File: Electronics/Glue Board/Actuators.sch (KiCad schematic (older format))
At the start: 4 parts, among them Q1 CSD17501Q5A, U1 PCA9685PW, U2 DRV8870DDA, U3 VNH5019A-E

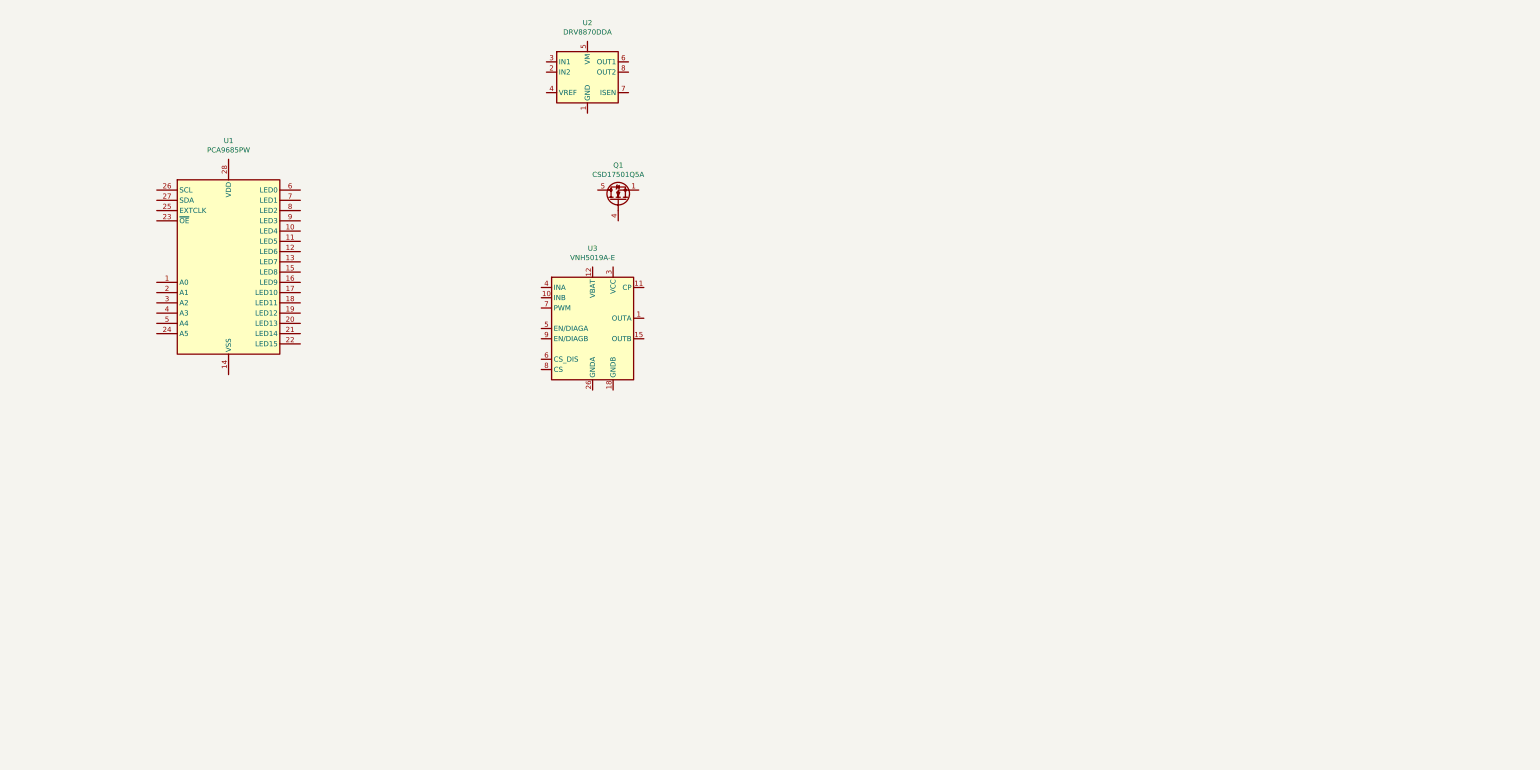
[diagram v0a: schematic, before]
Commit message: Finished the schematic for the most parts
Finished the schematic for the most parts
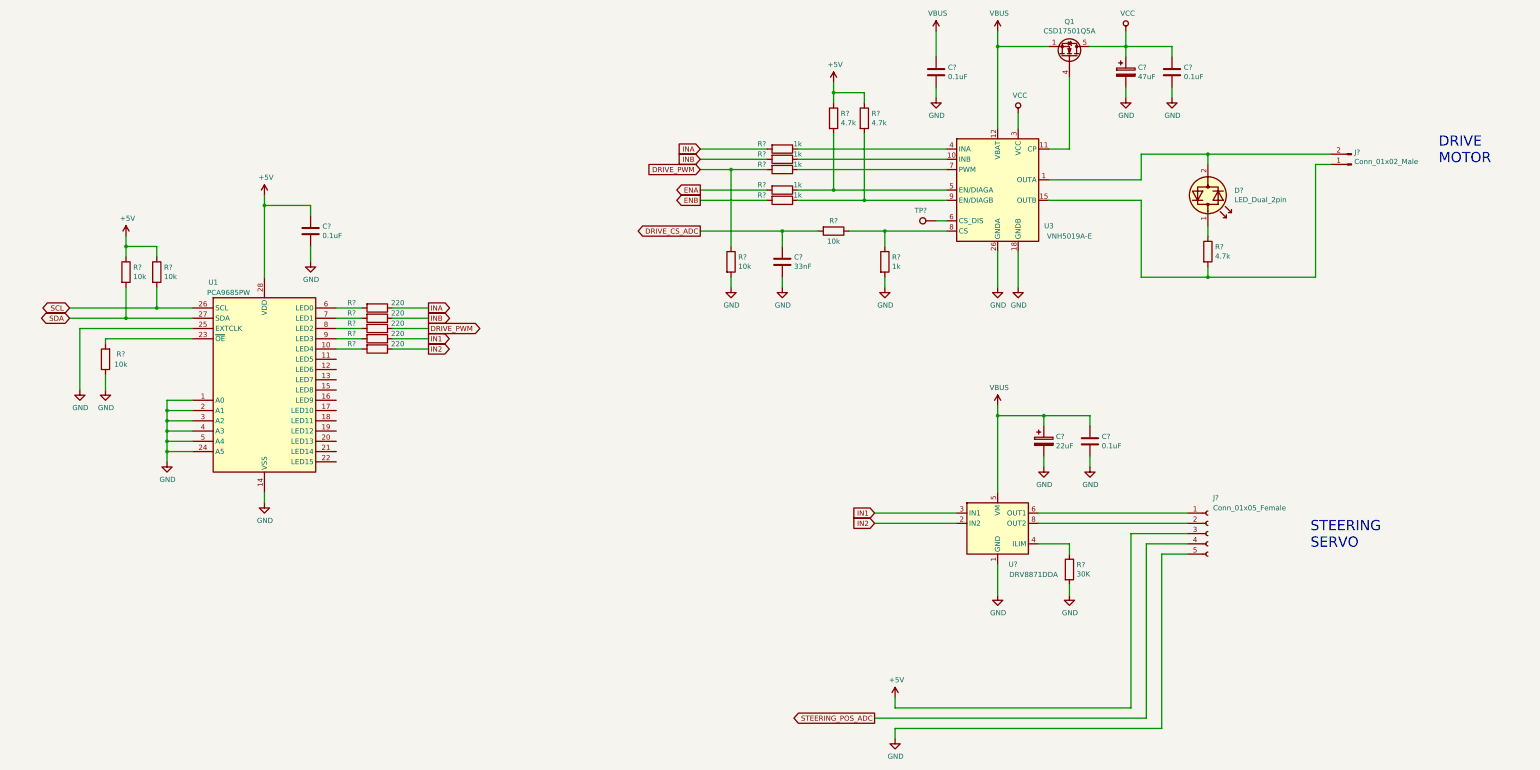
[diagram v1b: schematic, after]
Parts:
- removed U2: DRV8870DDA, Package_SO:Texas_HTSOP-8-1EP_3.9x4.9mm_P1.27mm_EP2.95x4.9mm_Mask2.4x3.1mm_ThermalVias, symbol Driver_Motor:DRV8870DDA
- added C?: 47uF, symbol Device:CP
- added C? (x4): 0.1uF, symbol Device:C
- added C?: 33nF, symbol Device:C
- added C?: 22uF, symbol Device:CP
- added D?: LED_Dual_2pin, symbol Device:LED_Dual_2pin
- added J?: Conn_01x02_Male, symbol Connector:Conn_01x02_Male
- added J?: Conn_01x05_Female, symbol Connector:Conn_01x05_Female
- added R? (x6): 1k, symbol Device:R
- added R? (x5): 10k, symbol Device:R
- added R? (x3): 4.7k, symbol Device:R
- added R?: 30K, symbol Device:R
- added R? (x5): 220, symbol Device:R
- added TP?: TestPoint, symbol Connector:TestPoint
- added U?: DRV8871DDA, Package_SO:Texas_HTSOP-8-1EP_3.9x4.9mm_P1.27mm_EP2.95x4.9mm_Mask2.4x3.1mm_ThermalVias, symbol Driver_Motor:DRV8871DDA
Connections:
- net GND: now reaches U1.1 (A0)
- net GND: now also U1.14 (VSS), U1.2 (A1), U1.24 (A5), U1.25 (EXTCLK), U1.3 (A2), U1.4 (A3), U1.5 (A4), U3.18 (GNDB), U3.19 (GNDB), U3.20 (GNDB), U3.26 (GNDA), U3.27 (GNDA), U3.28 (GNDA), C?.2, C?.2, C?.2, C?.2, C?.2, C?.2, C?.2, J?.5 (Pin_5), R?.1, R?.2, R?.2, R?.2, U?.1 (GND), U?.7 (GND), U?.9 (GND)
- net at U1.10 (LED4): now also R?.2
- net at U1.23 (~OE): now also R?.2
- net SCL: now reaches U1.26 (SCL)
- net SCL: now also R?.2
- net SDA: now reaches U1.27 (SDA)
- net SDA: now also R?.2
- net +5V: now reaches U1.28 (VDD)
- net +5V: now also C?.1, J?.3 (Pin_3), R?.1, R?.1, R?.1, R?.1
- net at U1.6 (LED0): now also R?.2
- net at U1.7 (LED1): now also R?.2
- net at U1.8 (LED2): now also R?.2
- net at U1.9 (LED3): now also R?.2
- net at U3.1 (OUTA), U3.25 (OUTA), U3.30 (OUTA)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: now also D?.2 (AK), J?.2 (Pin_2)
- net at U3.10 (INB): now also R?.1
- net at U3.11 (CP): now also Q1.4 (G)
- net VBUS: now reaches U3.12 (VBAT)
- net VBUS: now also Q1.1 (S), Q1.2 (S), Q1.3 (S), C?.1, C?.1, C?.1, U?.5 (VM)
- net VCC: now reaches U3.13 (VCC), U3.23 (VCC), U3.3 (VCC), U3.31 (VCC)
- net VCC: now also Q1.5 (D), C?.1, C?.1
- net at U3.15 (OUTB), U3.16 (OUTB), U3.21 (OUTB)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: now also J?.1 (Pin_1), R?.2
- net at U3.4 (INA): now also R?.1
- net at U3.5 (EN/DIAGA): now also R?.1, R?.2
- net at U3.6 (CS_DIS): now also TP?.1
- net at U3.7 (PWM): now also R?.1
- net at U3.8 (CS): now also R?.1, R?.1
- net at U3.9 (EN/DIAGB): now also R?.1, R?.2
- new net: D?.1 (KA), R?.1
- new net: R?.1, U?.4 (ILIM)
- new net: J?.1 (Pin_1), U?.6 (OUT1)
- new net: J?.2 (Pin_2), U?.8 (OUT2)
- new net DRIVE_CS_ADC: C?.1, R?.2
- new net DRIVE_PWM: R?.1, R?.1, R?.2
- new net ENA: R?.2
- new net ENB: R?.2
- new net IN1: R?.1, U?.3 (IN1)
- new net IN2: R?.1, U?.2 (IN2)
- new net INA: R?.1, R?.2
- new net INB: R?.1, R?.2
- new net STEERING_POS_ADC: J?.4 (Pin_4)
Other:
- note added: "DRIVE\nMOTOR"
- note added: "STEERING\nSERVO"
- moved on the sheet: Q1, U1, U3

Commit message: Complete Schematic and BOM
Complete Schematic and BOM. Next up, layout!
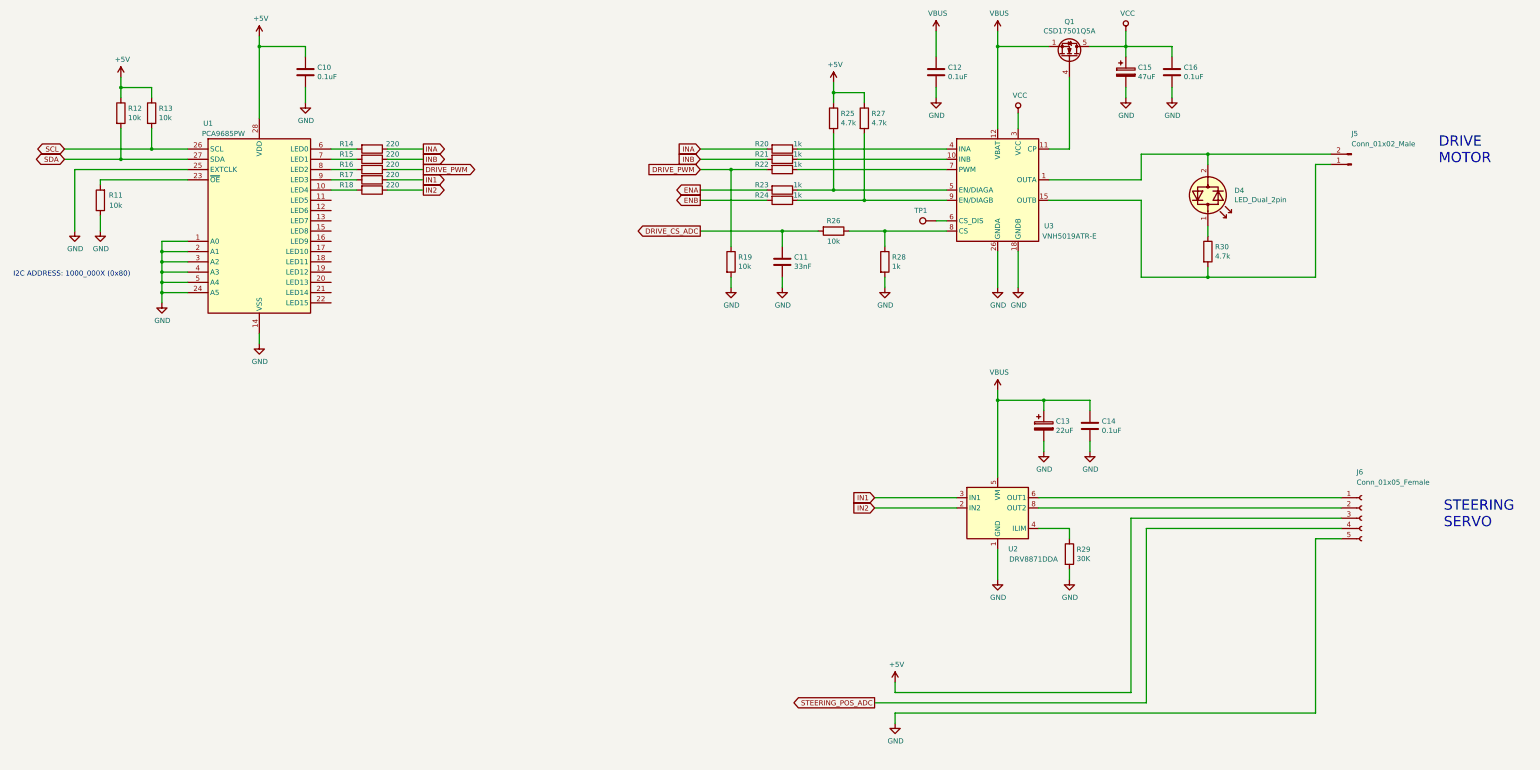
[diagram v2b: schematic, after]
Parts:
- C10, C12, C14, C16: renamed from C?; footprint (none) -> Capacitor_SMD:C_0805_2012Metric; MPN (none) -> C0805C104Z5VACTU
- C11: renamed from C?; footprint (none) -> Capacitor_SMD:C_0805_2012Metric; MPN (none) -> C0805C333K5RACTU
- C13: renamed from C?; footprint (none) -> Capacitor_SMD:C_1210_3225Metric; MPN (none) -> C1210C226K3PACTU
- C15: renamed from C?; footprint (none) -> Capacitor_SMD:C_1210_3225Metric; MPN (none) -> GRM32EC81C476KE15L
- D4: renamed from D?; footprint (none) -> LED_SMD:LED_1206_3216Metric; MPN (none) -> LTST-C235KGKRKT
- J5: renamed from J?; footprint (none) -> Connector_JST:JST_XH_B2B-XH-AM_1x02_P2.50mm_Vertical; MPN (none) -> B2B-XH-A(LF)(SN)
- J6: renamed from J?; footprint (none) -> Connector_Molex:Molex_PicoBlade_53047-0510_1x05_P1.25mm_Vertical; MPN (none) -> 0530470510
- Q1: MPN (none) -> CSD17501Q5A
- R11, R12, R13, R19, R26: renamed from R?; footprint (none) -> Resistor_SMD:R_0603_1608Metric; MPN (none) -> RC0603FR-0710KL
- R14, R15, R16, R17, R18: renamed from R?; footprint (none) -> Resistor_SMD:R_0603_1608Metric; MPN (none) -> CRGCQ0603F220R
- R20, R21, R22, R23, R24, R28: renamed from R?; footprint (none) -> Resistor_SMD:R_0603_1608Metric; MPN (none) -> RC0603JR-071KL
- R25, R27, R30: renamed from R?; footprint (none) -> Resistor_SMD:R_0603_1608Metric; MPN (none) -> ERJ-3EKF4751V
- R29: renamed from R?; footprint (none) -> Resistor_SMD:R_0603_1608Metric; MPN (none) -> ERA-3AEB303V
- TP1: renamed from TP?; footprint (none) -> TestPoint:TestPoint_Pad_D2.0mm
- U1: MPN (none) -> PCA9685PW
- U2: renamed from U?; MPN (none) -> DRV8871DDAR
- U3: value VNH5019A-E -> VNH5019ATR-E; MPN (none) -> VNH5019ATR-E
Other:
- note added: "I2C ADDRESS: 1000_000X (0x80)"
- moved on the sheet: C10, C13, C14, J6, R11, R12, R13, R14, R15, R16, R17, R18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

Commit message: Added Motor v-sense and battery mon. Layout time!
Added Motor v-sense and battery mon. Layout time!
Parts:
- removed R14, R15, R16, R17, R18: 220, Resistor_SMD:R_0603_1608Metric, symbol Device:R
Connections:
- net DRIVE_PWM: now also U1.8 (LED2)
- net IN1: now also U1.9 (LED3)
- net IN2: now also U1.10 (LED4)
- net INA: now also U1.6 (LED0)
- net INB: now also U1.7 (LED1)
- net OUTA: now reaches D4.2 (AK), U3.1 (OUTA), U3.25 (OUTA), U3.30 (OUTA), U3.33 (OUTA)
- net OUTA: now also J5.1 (Pin_1); no longer J5.2 (Pin_2)
- net OUTB: now reaches R30.2, U3.15 (OUTB), U3.16 (OUTB), U3.21 (OUTB), U3.32 (OUTB)
- net OUTB: now also J5.2 (Pin_2); no longer J5.1 (Pin_1)
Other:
- moved on the sheet: J5
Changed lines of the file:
@@
 L Connector:Conn_01x02_Male J5
 U 1 1 5E201F91
-P 14650 2700
-F 0 "J5" H 14650 2400 50  0000 R CNN
-F 1 "Conn_01x02_Male" H 14650 2500 50  0000 R CNN
-F 2 "Connector_JST:JST_XH_B2B-XH-AM_1x02_P2.50mm_Vertical" H 14650 2700 50  0001 C CNN
-F 3 "~" H 14650 2700 50  0001 C CNN
-F 4 "B2B-XH-A(LF)(SN)" H 14650 2700 50  0001 C CNN "MPN"
-	1    14650 2700
-	-1   0    0    1
+P 14700 2600
+F 0 "J5" H 14800 2800 50  0000 R CNN
+F 1 "Conn_01x02_Male" H 14800 2700 50  0000 R CNN
+F 2 "Connector_JST:JST_XH_B2B-XH-AM_1x02_P2.50mm_Vertical" H 14700 2600 50  0001 C CNN
+F 3 "~" H 14700 2600 50  0001 C CNN
+F 4 "B2B-XH-A(LF)(SN)" H 14700 2600 50  0001 C CNN "MPN"
+	1    14700 2600
+	-1   0    0    -1
 $EndComp
 $Comp
@@
 Wire Wire Line
 	13250 2700 13250 2600
-Connection ~ 13250 2600
 Wire Wire Line
 	13250 2600 12600 2600
@@
 Wire Wire Line
 	13250 3800 14300 3800
-Wire Wire Line
-	13250 2600 14450 2600
-Wire Wire Line
-	14450 2700 14300 2700
 Wire Wire Line
 	14300 2700 14300 3800
@@
 Wire Wire Line
 	4450 1950 4450 2100
-$Comp
-L Device:R R14
-U 1 1 5E2E4897
-P 5100 2550
-F 0 "R14" V 5050 2300 50  0000 C CNN
-F 1 "220" V 5050 2750 50  0000 C CNN
-F 2 "Resistor_SMD:R_0603_1608Metric" V 5030 2550 50  0001 C CNN
-F 3 "~" H 5100 2550 50  0001 C CNN
-F 4 "CRGCQ0603F220R" V 5100 2550 50  0001 C CNN "MPN"
-	1    5100 2550
-	0    1    1    0
-$EndComp
-$Comp
-L Device:R R15
-U 1 1 5E2E5029
-P 5100 2650
-F 0 "R15" V 5050 2400 50  0000 C CNN
-F 1 "220" V 5050 2850 50  0000 C CNN
-F 2 "Resistor_SMD:R_0603_1608Metric" V 5030 2650 50  0001 C CNN
-F 3 "~" H 5100 2650 50  0001 C CNN
-F 4 "CRGCQ0603F220R" V 5100 2650 50  0001 C CNN "MPN"
-	1    5100 2650
-	0    1    1    0
-$EndComp
-$Comp
-L Device:R R16
-U 1 1 5E2E53A1
-P 5100 2750
-F 0 "R16" V 5050 2500 50  0000 C CNN
-F 1 "220" V 5050 2950 50  0000 C CNN
-F 2 "Resistor_SMD:R_0603_1608Metric" V 5030 2750 50  0001 C CNN
-F 3 "~" H 5100 2750 50  0001 C CNN
-F 4 "CRGCQ0603F220R" V 5100 2750 50  0001 C CNN "MPN"
-	1    5100 2750
-	0    1    1    0
-$EndComp
-$Comp
-L Device:R R17
-U 1 1 5E2E5671
-P 5100 2850
-F 0 "R17" V 5050 2600 50  0000 C CNN
-F 1 "220" V 5050 3050 50  0000 C CNN
-F 2 "Resistor_SMD:R_0603_1608Metric" V 5030 2850 50  0001 C CNN
-F 3 "~" H 5100 2850 50  0001 C CNN
-F 4 "CRGCQ0603F220R" V 5100 2850 50  0001 C CNN "MPN"
-	1    5100 2850
-	0    1    1    0
-$EndComp
-$Comp
-L Device:R R18
-U 1 1 5E2E5899
-P 5100 2950
-F 0 "R18" V 5050 2700 50  0000 C CNN
-F 1 "220" V 5050 3150 50  0000 C CNN
-F 2 "Resistor_SMD:R_0603_1608Metric" V 5030 2950 50  0001 C CNN
-F 3 "~" H 5100 2950 50  0001 C CNN
-F 4 "CRGCQ0603F220R" V 5100 2950 50  0001 C CNN "MPN"
-	1    5100 2950
-	0    1    1    0
-$EndComp
-Wire Wire Line
-	4700 2550 4950 2550
-Wire Wire Line
-	4700 2650 4950 2650
-Wire Wire Line
-	4950 2750 4700 2750
-Wire Wire Line
-	4700 2850 4950 2850
-Wire Wire Line
-	4950 2950 4700 2950
-Text GLabel 5600 2550 2    50   Output ~ 0
+Text GLabel 5300 2550 2    50   Output ~ 0
 INA
-Text GLabel 5600 2650 2    50   Output ~ 0
+Text GLabel 5300 2650 2    50   Output ~ 0
 INB
-Text GLabel 5600 2750 2    50   Output ~ 0
+Text GLabel 5300 2750 2    50   Output ~ 0
 DRIVE_PWM
-Text GLabel 5600 2850 2    50   Output ~ 0
+Text GLabel 5300 2850 2    50   Output ~ 0
 IN1
-Text GLabel 5600 2950 2    50   Output ~ 0
+Text GLabel 5300 2950 2    50   Output ~ 0
 IN2
-Wire Wire Line
-	5250 2550 5600 2550
-Wire Wire Line
-	5600 2650 5250 2650
-Wire Wire Line
-	5250 2750 5600 2750
-Wire Wire Line
-	5600 2850 5250 2850
-Wire Wire Line
-	5250 2950 5600 2950
 Text GLabel 10000 7950 0    50   Output ~ 0
 STEERING_POS_ADC
@@
 Wire Wire Line
 	10200 7850 12500 7850
-Text Notes 15500 2700 0    100  ~ 0
+Text Notes 15500 2800 0    100  ~ 0
 DRIVE\nMOTOR
 Text Notes 15550 6250 0    100  ~ 0
@@
 Wire Wire Line
 	11600 5950 14550 5950
+Text GLabel 12650 3050 2    50   Input ~ 0
+OUTB
+Text GLabel 12650 2850 2    50   Input ~ 0
+OUTA
+Wire Wire Line
+	12600 2850 12650 2850
+Connection ~ 12600 2850
+Wire Wire Line
+	12600 3050 12650 3050
+Connection ~ 12600 3050
+Wire Wire Line
+	14500 2700 14300 2700
+Wire Wire Line
+	13250 2600 14500 2600
+Connection ~ 13250 2600
+Wire Wire Line
+	4700 2550 5300 2550
+Wire Wire Line
+	4700 2650 5300 2650
+Wire Wire Line
+	4700 2750 5300 2750
+Wire Wire Line
+	4700 2850 5300 2850
+Wire Wire Line
+	4700 2950 5300 2950
 $EndSCHEMATC

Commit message: Updated Readme
Updated Readme
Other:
- note added: "PWM DRIVER - PCA9685PW\n\nI2C ADDRESS: 1000_000X (0x80)\nSHIFTED ADY: 0100_1000 (0x40)"
- note removed: "I2C ADDRESS: 1000_000X (0x80)"
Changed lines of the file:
@@
 Text Notes 15550 6250 0    100  ~ 0
 STEERING\nSERVO
-Text Notes 1600 3800 0    50   ~ 0
-I2C ADDRESS: 1000_000X (0x80)
+Text Notes 1550 4100 0    50   ~ 0
+PWM DRIVER - PCA9685PW\n\nI2C ADDRESS: 1000_000X (0x80)\nSHIFTED ADY: 0100_1000  (0x40)
 Wire Wire Line
 	10200 8050 14300 8050

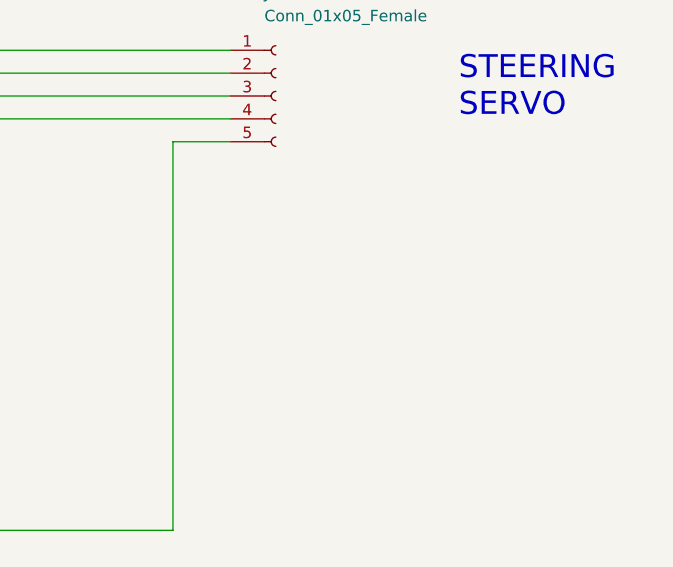
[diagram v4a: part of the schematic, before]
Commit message: Added harnessing and assembly diagrams
Added harnessing and assembly diagrams
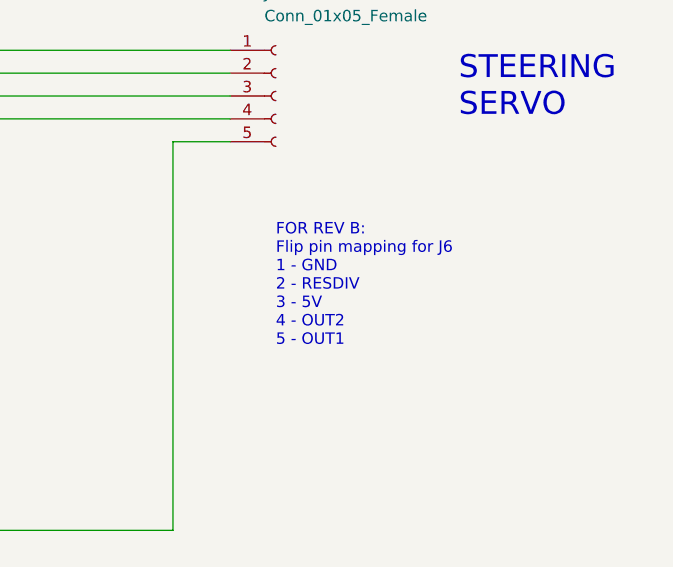
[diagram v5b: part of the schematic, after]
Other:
- note added: "FOR REV B:\nFlip pin mapping for J6\n1 - GND\n2 - RESDIV\n3 - 5V\n4 - OUT2\n5 - OUT1"
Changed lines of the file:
@@
 Wire Wire Line
 	4700 2950 5300 2950
+Text Notes 14750 7250 0    50   ~ 0
+FOR REV B:\nFlip pin mapping for J6\n1 - GND\n2 - RESDIV\n3 - 5V\n4 - OUT2\n5 - OUT1
 $EndSCHEMATC
